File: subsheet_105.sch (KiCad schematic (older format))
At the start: 5 parts, among them J100 Power

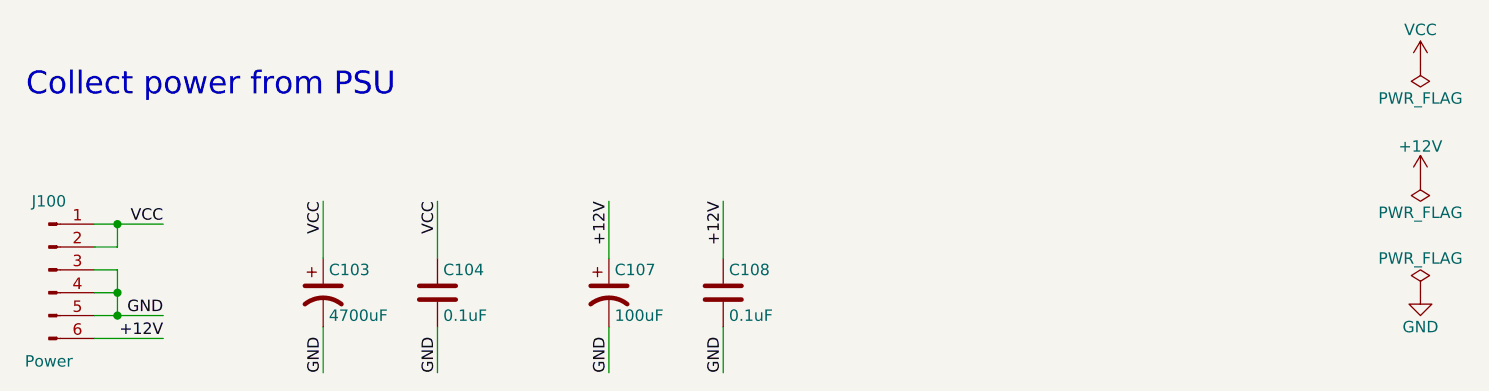
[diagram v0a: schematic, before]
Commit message: Resolves #10 : Remove the C103
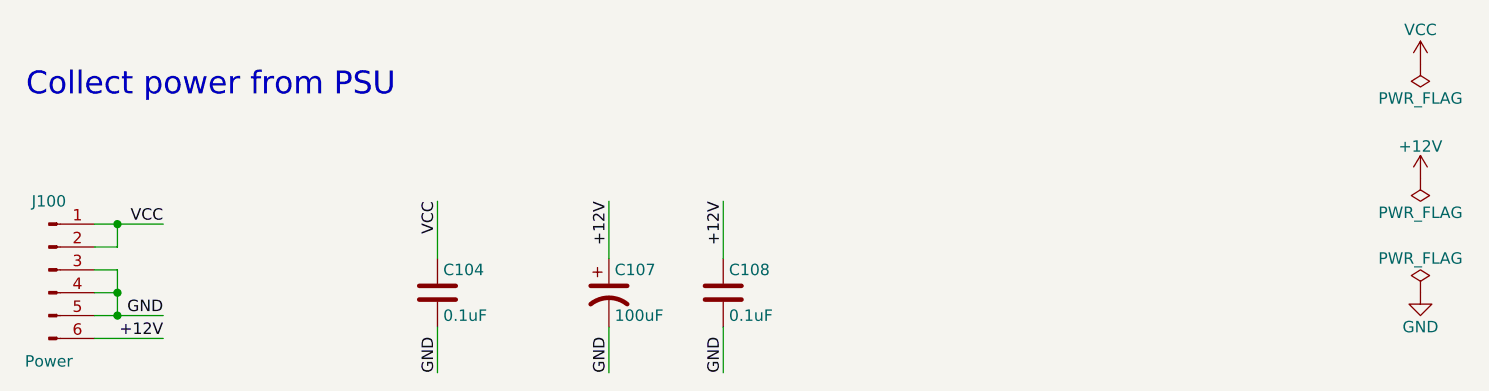
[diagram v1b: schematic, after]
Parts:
- removed C103: 4700uF, commons_passives_THT:Passive_THT_capacitor_polarized_W16.51mm_L45.72mm, symbol Device:CP1
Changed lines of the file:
@@
-$EndComp
-$Comp
-L Device:CP1 C103
-U 1 1 6079D92A
-P 2500 2000
-F 0 "C103" H 2525 2100 50  0000 L CNN
-F 1 "4700uF" H 2525 1900 50  0000 L CNN
-F 2 "commons_passives_THT:Passive_THT_capacitor_polarized_W16.51mm_L45.72mm" H 2500 2000 50  0001 C CNN
-F 3 "~" H 2500 2000 50  0001 C CNN
-	1    2500 2000
-	1    0    0    -1
 $EndComp
 $Comp
@@
 Text Label 3000 1600 3    50   ~ 0
 VCC
-Text Label 2500 1600 3    50   ~ 0
-VCC
 Text Label 4250 1600 3    50   ~ 0
 +12V
@@
 GND
 Text Label 3000 2350 1    50   ~ 0
-GND
-Text Label 2500 2350 1    50   ~ 0
 GND
 Text Notes 1200 1150 0    100  ~ 0
@@
 	1500 2200 1800 2200
 Wire Wire Line
-	2500 1850 2500 1600
-Wire Wire Line
 	3000 1850 3000 1600
 Wire Wire Line
@@
 	4250 1850 4250 1600
 Wire Wire Line
-	2500 2350 2500 2150
-Wire Wire Line
 	3000 2350 3000 2150

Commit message: Resolves #12 : Use the reference 'CP?' for polarized capacitors
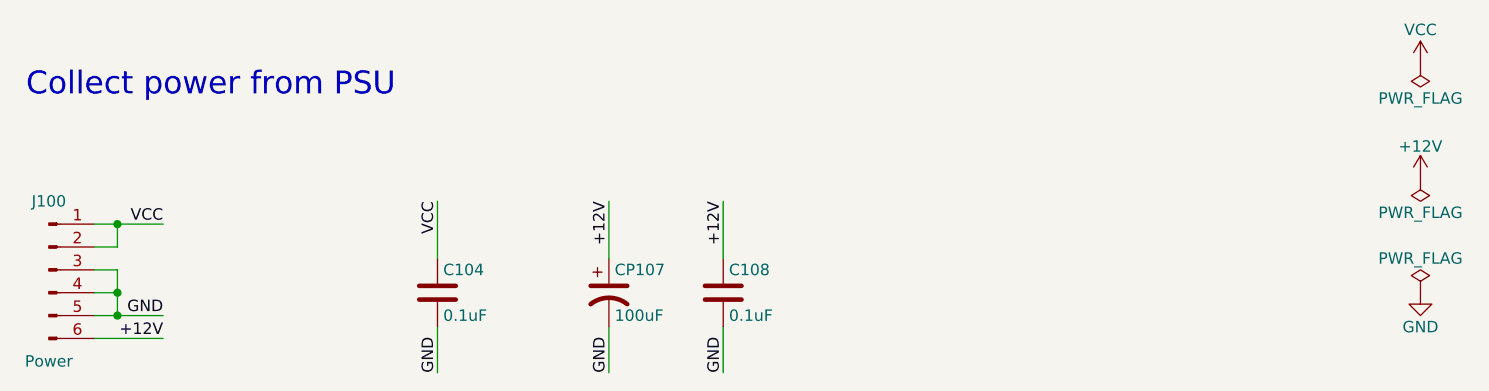
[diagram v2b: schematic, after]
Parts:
- renumbered C107 to CP107
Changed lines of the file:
@@
 $EndComp
 $Comp
-L Device:CP1 C107
+L Device:CP1 CP107
 U 1 1 6079EFD5
 P 3750 2000
-F 0 "C107" H 3775 2100 50  0000 L CNN
+F 0 "CP107" H 3775 2100 50  0000 L CNN
 F 1 "100uF" H 3775 1900 50  0000 L CNN
 F 2 "commons_passives_THT:Passive_THT_capacitor_polarized_W6.35mm_L20.32mm" H 3750 2000 50  0001 C CNN

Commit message: Resolves #8 : Assign 1206 hand-solder footprints to non polarized capacitors
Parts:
- C104, C108: footprint commons_passives_THT:Passive_THT_capacitor_mlcc_W2.54mm_L7.62mm -> Capacitor_SMD:C_1206_3216Metric_Pad1.33x1.80mm_HandSolder
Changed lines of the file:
@@
 F 0 "C104" H 3025 2100 50  0000 L CNN
 F 1 "0.1uF" H 3025 1900 50  0000 L CNN
-F 2 "commons_passives_THT:Passive_THT_capacitor_mlcc_W2.54mm_L7.62mm" H 3038 1850 50  0001 C CNN
+F 2 "Capacitor_SMD:C_1206_3216Metric_Pad1.33x1.80mm_HandSolder" H 3038 1850 50  0001 C CNN
 F 3 "~" H 3000 2000 50  0001 C CNN
 	1    3000 2000
@@
 F 0 "C108" H 4275 2100 50  0000 L CNN
 F 1 "0.1uF" H 4275 1900 50  0000 L CNN
-F 2 "commons_passives_THT:Passive_THT_capacitor_mlcc_W2.54mm_L7.62mm" H 4288 1850 50  0001 C CNN
+F 2 "Capacitor_SMD:C_1206_3216Metric_Pad1.33x1.80mm_HandSolder" H 4288 1850 50  0001 C CNN
 F 3 "~" H 4250 2000 50  0001 C CNN
 	1    4250 2000

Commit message: Resolves #9 : Assign radial THT footprints to polarized capacitors
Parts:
- CP107: footprint commons_passives_THT:Passive_THT_capacitor_polarized_W6.35mm_L20.32mm -> Capacitor_THT:C_Radial_D8.0mm_H11.5mm_P3.50mm
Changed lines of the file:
@@
 F 0 "CP107" H 3775 2100 50  0000 L CNN
 F 1 "100uF" H 3775 1900 50  0000 L CNN
-F 2 "commons_passives_THT:Passive_THT_capacitor_polarized_W6.35mm_L20.32mm" H 3750 2000 50  0001 C CNN
+F 2 "Capacitor_THT:C_Radial_D8.0mm_H11.5mm_P3.50mm" H 3750 2000 50  0001 C CNN
 F 3 "~" H 3750 2000 50  0001 C CNN
 	1    3750 2000
